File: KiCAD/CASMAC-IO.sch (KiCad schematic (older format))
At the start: 19 parts, among them U2 74LS04, U3 74LS138, U6 74LS573

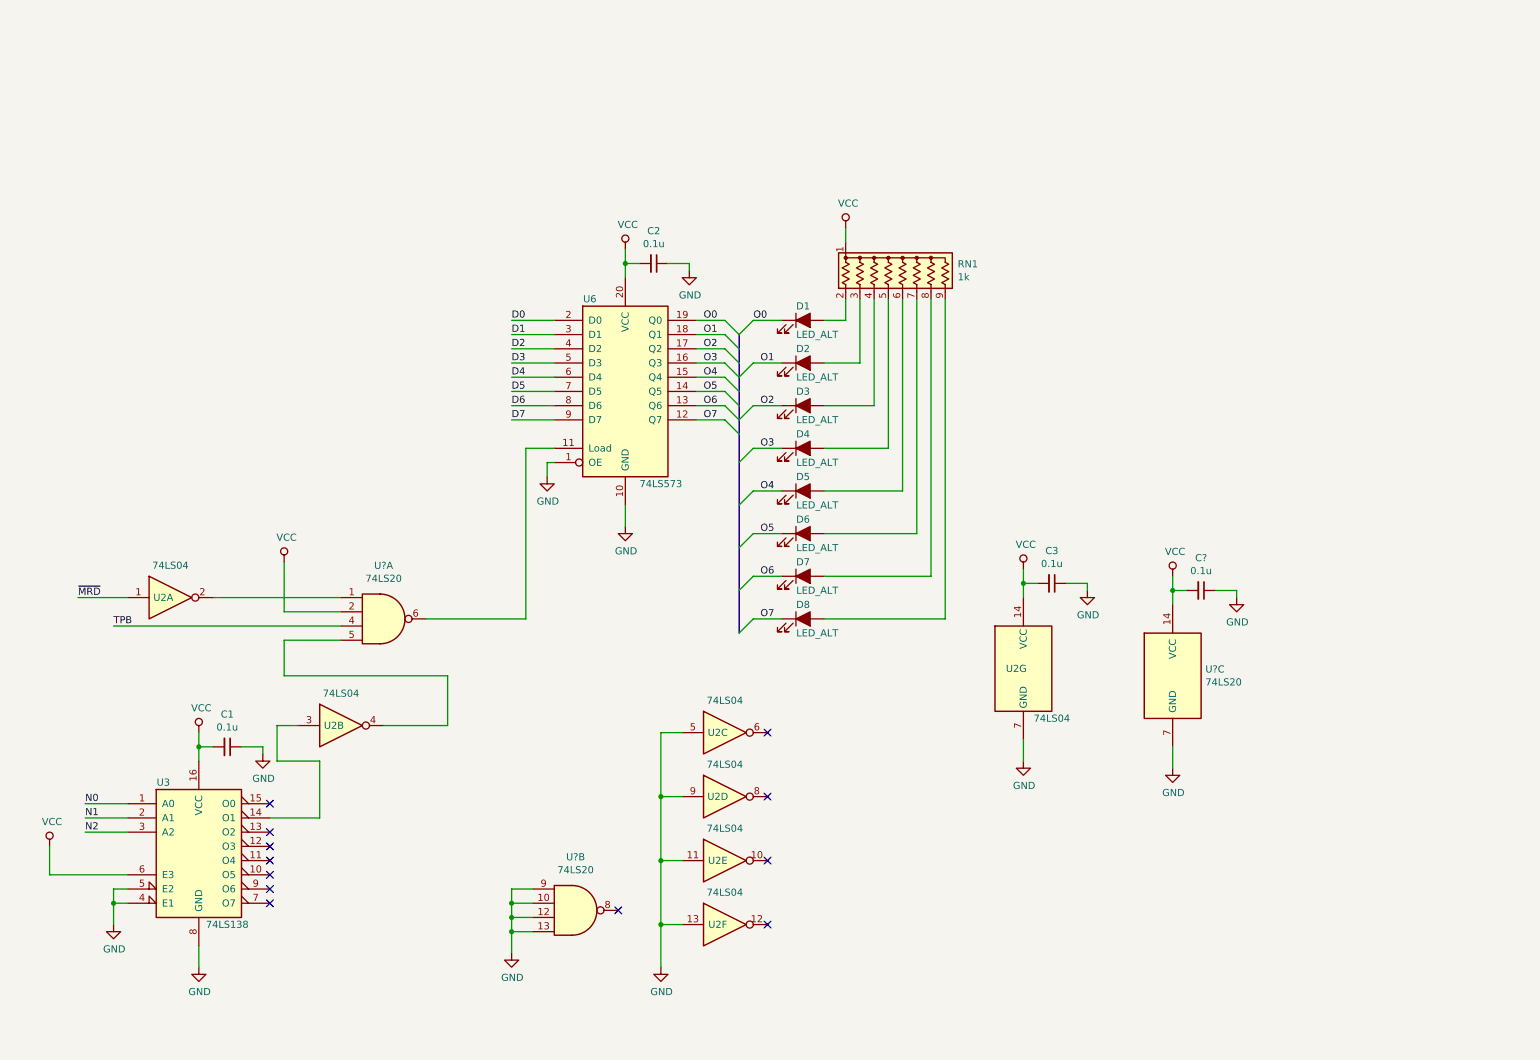
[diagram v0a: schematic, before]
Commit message: ロジックICを74HCシリーズへ統一
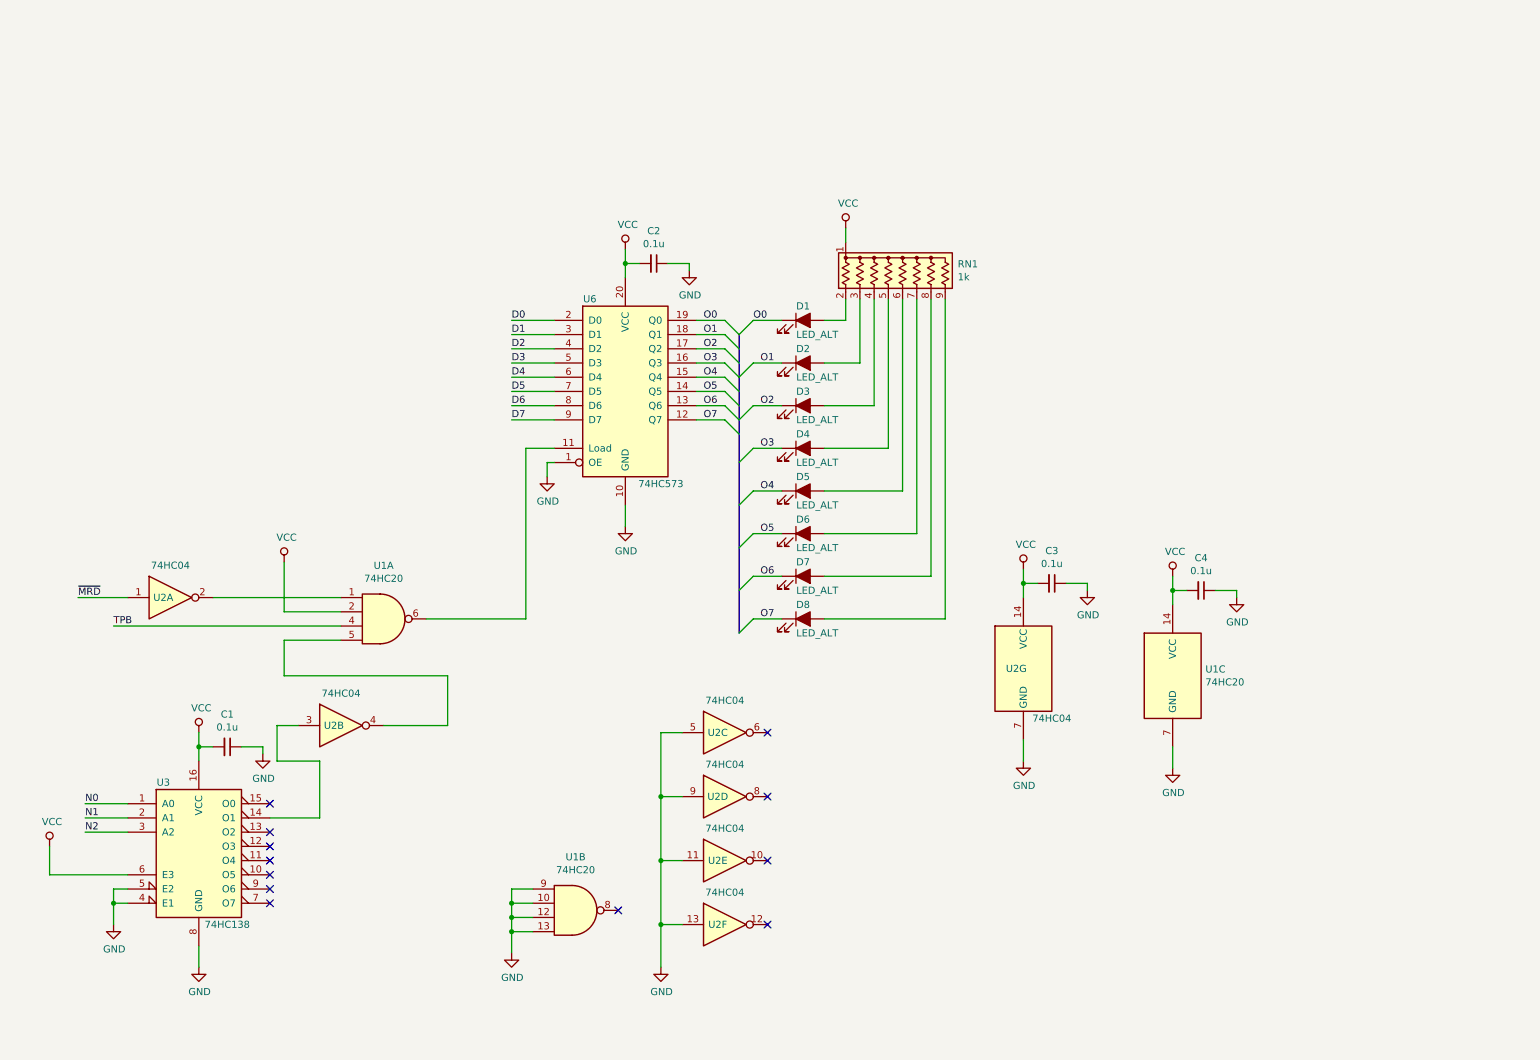
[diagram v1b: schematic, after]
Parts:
- U1: renamed from U?; value 74LS20 -> 74HC20
- U2: value 74LS04 -> 74HC04
- U3: value 74LS138 -> 74HC138
- U6: value 74LS573 -> 74HC573
- gave numbers to parts that had none: 1
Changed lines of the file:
@@
 EESchema Schematic File Version 4
+LIBS:CASMAC-IO-cache
 EELAYER 30 0
 EELAYER END
@@
 P 1800 6300
 F 0 "U3" H 1550 6750 50  0000 C CNN
-F 1 "74LS138" H 2000 5750 50  0000 C CNN
+F 1 "74HC138" H 2000 5750 50  0000 C CNN
 F 2 "" H 1800 6300 50  0001 C CNN
 F 3 "http://www.ti.com/lit/gpn/sn74LS138" H 1800 6300 50  0001 C CNN
@@
 P 4800 3100
 F 0 "U6" H 4550 3750 50  0000 C CNN
-F 1 "74LS573" H 5050 2450 50  0000 C CNN
+F 1 "74HC573" H 5050 2450 50  0000 C CNN
 F 2 "" H 4800 3100 50  0001 C CNN
 F 3 "74xx/74hc573.pdf" H 4800 3100 50  0001 C CNN
@@
 P 1600 4550
 F 0 "U2" H 1550 4550 50  0000 C CNN
-F 1 "74LS04" H 1600 4776 50  0000 C CNN
+F 1 "74HC04" H 1600 4776 50  0000 C CNN
 F 2 "" H 1600 4550 50  0001 C CNN
 F 3 "http://www.ti.com/lit/gpn/sn74LS04" H 1600 4550 50  0001 C CNN
@@
 P 2800 5450
 F 0 "U2" H 2750 5450 50  0000 C CNN
-F 1 "74LS04" H 2800 5676 50  0000 C CNN
+F 1 "74HC04" H 2800 5676 50  0000 C CNN
 F 2 "" H 2800 5450 50  0001 C CNN
 F 3 "http://www.ti.com/lit/gpn/sn74LS04" H 2800 5450 50  0001 C CNN
@@
 P 5500 5500
 F 0 "U2" H 5450 5500 50  0000 C CNN
-F 1 "74LS04" H 5500 5726 50  0000 C CNN
+F 1 "74HC04" H 5500 5726 50  0000 C CNN
 F 2 "" H 5500 5500 50  0001 C CNN
 F 3 "http://www.ti.com/lit/gpn/sn74LS04" H 5500 5500 50  0001 C CNN
@@
 P 5500 5950
 F 0 "U2" H 5450 5950 50  0000 C CNN
-F 1 "74LS04" H 5500 6176 50  0000 C CNN
+F 1 "74HC04" H 5500 6176 50  0000 C CNN
 F 2 "" H 5500 5950 50  0001 C CNN
 F 3 "http://www.ti.com/lit/gpn/sn74LS04" H 5500 5950 50  0001 C CNN
@@
 P 5500 6400
 F 0 "U2" H 5450 6400 50  0000 C CNN
-F 1 "74LS04" H 5500 6626 50  0000 C CNN
+F 1 "74HC04" H 5500 6626 50  0000 C CNN
 F 2 "" H 5500 6400 50  0001 C CNN
 F 3 "http://www.ti.com/lit/gpn/sn74LS04" H 5500 6400 50  0001 C CNN
@@
 P 5500 6850
 F 0 "U2" H 5450 6850 50  0000 C CNN
-F 1 "74LS04" H 5500 7076 50  0000 C CNN
+F 1 "74HC04" H 5500 7076 50  0000 C CNN
 F 2 "" H 5500 6850 50  0001 C CNN
 F 3 "http://www.ti.com/lit/gpn/sn74LS04" H 5500 6850 50  0001 C CNN
@@
 P 7600 5050
 F 0 "U2" H 7550 5050 50  0000 C CNN
-F 1 "74LS04" H 7800 4700 50  0000 C CNN
+F 1 "74HC04" H 7800 4700 50  0000 C CNN
 F 2 "" H 7600 5050 50  0001 C CNN
 F 3 "http://www.ti.com/lit/gpn/sn74LS04" H 7600 5050 50  0001 C CNN
@@
 	2300 6100 2650 6100
 $Comp
-L power:GND #PWR?
+L power:GND #PWR016
 U 1 1 609AF621
 P 4250 3700
-F 0 "#PWR?" H 4250 3450 50  0001 C CNN
+F 0 "#PWR016" H 4250 3450 50  0001 C CNN
 F 1 "GND" H 4255 3527 50  0000 C CNN
 F 2 "" H 4250 3700 50  0001 C CNN
@@
 	4250 3600 4300 3600
 $Comp
-L 74xx:74LS20 U?
+L 74xx:74LS20 U1
 U 1 1 609E0917
 P 3100 4700
-F 0 "U?" H 3100 5075 50  0000 C CNN
-F 1 "74LS20" H 3100 4984 50  0000 C CNN
+F 0 "U1" H 3100 5075 50  0000 C CNN
+F 1 "74HC20" H 3100 4984 50  0000 C CNN
 F 2 "" H 3100 4700 50  0001 C CNN
 F 3 "http://www.ti.com/lit/gpn/sn74LS20" H 3100 4700 50  0001 C CNN
@@
 $EndComp
 $Comp
-L 74xx:74LS20 U?
+L 74xx:74LS20 U1
 U 2 1 609E3CF1
 P 4450 6750
-F 0 "U?" H 4450 7125 50  0000 C CNN
-F 1 "74LS20" H 4450 7034 50  0000 C CNN
+F 0 "U1" H 4450 7125 50  0000 C CNN
+F 1 "74HC20" H 4450 7034 50  0000 C CNN
 F 2 "" H 4450 6750 50  0001 C CNN
 F 3 "http://www.ti.com/lit/gpn/sn74LS20" H 4450 6750 50  0001 C CNN
@@
 $EndComp
 $Comp
-L 74xx:74LS20 U?
+L 74xx:74LS20 U1
 U 3 1 609E5629
 P 8650 5100
-F 0 "U?" H 8880 5146 50  0000 L CNN
-F 1 "74LS20" H 8880 5055 50  0000 L CNN
+F 0 "U1" H 8880 5146 50  0000 L CNN
+F 1 "74HC20" H 8880 5055 50  0000 L CNN
 F 2 "" H 8650 5100 50  0001 C CNN
 F 3 "http://www.ti.com/lit/gpn/sn74LS20" H 8650 5100 50  0001 C CNN
@@
 $EndComp
 $Comp
-L power:VCC #PWR?
+L power:VCC #PWR017
 U 1 1 609E7963
 P 8650 4400
-F 0 "#PWR?" H 8650 4250 50  0001 C CNN
+F 0 "#PWR017" H 8650 4250 50  0001 C CNN
 F 1 "VCC" H 8667 4573 50  0000 C CNN
 F 2 "" H 8650 4400 50  0001 C CNN
@@
 $EndComp
 $Comp
-L Device:C_Small C?
+L Device:C_Small C4
 U 1 1 609E7969
 P 8850 4500
-F 0 "C?" V 8621 4500 50  0000 C CNN
+F 0 "C4" V 8621 4500 50  0000 C CNN
 F 1 "0.1u" V 8712 4500 50  0000 C CNN
 F 2 "" H 8850 4500 50  0001 C CNN
@@
 Connection ~ 8650 4500
 $Comp
-L power:GND #PWR?
+L power:GND #PWR019
 U 1 1 609E7973
 P 9100 4550
-F 0 "#PWR?" H 9100 4300 50  0001 C CNN
+F 0 "#PWR019" H 9100 4300 50  0001 C CNN
 F 1 "GND" H 9105 4377 50  0000 C CNN
 F 2 "" H 9100 4550 50  0001 C CNN
@@
 	9100 4500 9100 4550
 $Comp
-L power:GND #PWR?
+L power:GND #PWR018
 U 1 1 609EBFEE
 P 8650 5750
-F 0 "#PWR?" H 8650 5500 50  0001 C CNN
+F 0 "#PWR018" H 8650 5500 50  0001 C CNN
 F 1 "GND" H 8655 5577 50  0000 C CNN
 F 2 "" H 8650 5750 50  0001 C CNN
@@
 	2350 5450 2500 5450
 $Comp
-L power:VCC #PWR?
+L power:VCC #PWR03
 U 1 1 60A2BFA8
 P 2400 4300
-F 0 "#PWR?" H 2400 4150 50  0001 C CNN
+F 0 "#PWR03" H 2400 4150 50  0001 C CNN
 F 1 "VCC" H 2417 4473 50  0000 C CNN
 F 2 "" H 2400 4300 50  0001 C CNN

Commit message: 入力部分等 回路見直し
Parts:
- removed U1: 74HC20, symbol 74xx:74LS20
- removed U6: 74HC573, symbol 74xx:74LS573
- added C5, C6, C7: 0.1u, symbol Device:C_Small
- added J1: OUT-CON, symbol Connector_Generic:Conn_02x07_Odd_Even
- added J2: IN-CON, symbol Connector_Generic:Conn_02x07_Odd_Even
- added J3: CPU BUS, symbol Connector_Generic:Conn_02x20_Odd_Even
- added RN2: 10k, Resistor_THT:R_Array_SIP9, symbol Device:R_Network08_US
- added SW1: SW_DIP_x08, symbol Switch:SW_DIP_x08
- added U1, U5, U8: 74HC541, symbol 74xx:74LS541
- added U4: 74HC10, symbol 74xx:74LS10
- added U6: 74LS273, symbol 74xx:74LS273
- added U7: ULN2803A, symbol Transistor_Array:ULN2803A
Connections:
- net labels added: CLK, EO0, EO1, EO2, EO3, EO4, EO5, EO6, EO7, I0, I1, I2, I3, I4, I5, I6, I7, MA0, MA1, MA2, MA3, MA4, MA5, MA6, MA7, Q, SC0, SC1, TPA, VDD, ~CLEAR, ~DMA-IN, ~DMA-OUT, ~EF1, ~EF2, ~EF3, ~EF4, ~INT, ~MWR, ~WAIT, ~XTAL
- wire segments 110 -> 315
- no-connect marks 12 -> 41
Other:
- moved on the sheet: C1, C2, C3, C4, D1, D2, D3, D4, D5, D6, D7, D8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
